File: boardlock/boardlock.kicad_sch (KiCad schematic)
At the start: 0 parts

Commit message: update
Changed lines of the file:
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@@
 (kicad_sch (version 20230121) (generator eeschema)
   (paper "A4")
-  (sheet (at 62.23 140.97) (size 43.18 29.21) (fields_autoplaced)
+  (sheet (at 191.77 77.47) (size 43.18 29.21) (fields_autoplaced)
     (stroke (width 0.1524) (type solid))
     (fill (color 0 0 0 0.0000))
-    (property "Sheetname" "sensors" (at 62.23 140.2584 0)
+    (property "Sheetname" "sensors" (at 191.77 76.7584 0)
       (effects (font (size 1.27 1.27)) (justify left bottom))
     )
-    (property "Sheetfile" "sesnsors.kicad_sch" (at 62.23 170.7646 0)
+    (property "Sheetfile" "sesnsors.kicad_sch" (at 191.77 107.2646 0)
       (effects (font (size 1.27 1.27)) (justify left top))
     )
@@
     )
   )
-  (sheet (at 132.08 93.98) (size 40.64 24.13) (fields_autoplaced)
+  (sheet (at 191.77 128.27) (size 40.64 24.13) (fields_autoplaced)
     (stroke (width 0.1524) (type solid))
     (fill (color 0 0 0 0.0000))
-    (property "Sheetname" "audio" (at 132.08 93.2684 0)
+    (property "Sheetname" "audio" (at 191.77 127.5584 0)
       (effects (font (size 1.27 1.27)) (justify left bottom))
     )
-    (property "Sheetfile" "audio.kicad_sch" (at 132.08 118.6946 0)
+    (property "Sheetfile" "audio.kicad_sch" (at 191.77 152.9846 0)
       (effects (font (size 1.27 1.27)) (justify left top))
     )
@@
     )
   )
-  (sheet (at 60.96 34.29) (size 43.18 30.48) (fields_autoplaced)
+  (sheet (at 187.96 25.4) (size 43.18 30.48) (fields_autoplaced)
     (stroke (width 0.1524) (type solid))
     (fill (color 0 0 0 0.0000))
-    (property "Sheetname" "power" (at 60.96 33.5784 0)
+    (property "Sheetname" "power" (at 187.96 24.6884 0)
       (effects (font (size 1.27 1.27)) (justify left bottom))
     )
-    (property "Sheetfile" "power.kicad_sch" (at 60.96 65.3546 0)
+    (property "Sheetfile" "power.kicad_sch" (at 187.96 56.4646 0)
       (effects (font (size 1.27 1.27)) (justify left top))
     )

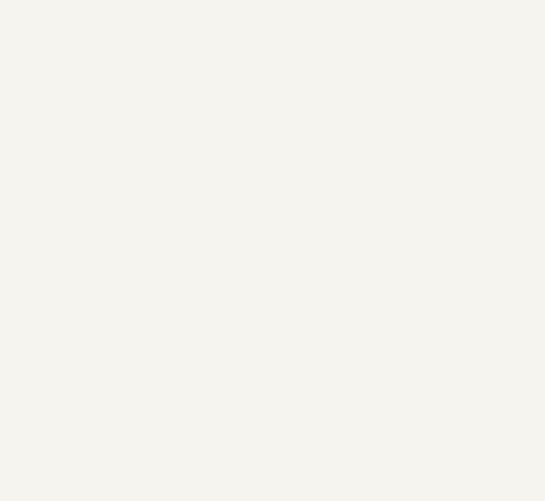
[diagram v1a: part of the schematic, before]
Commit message: Started adding IMU and GPS circuits
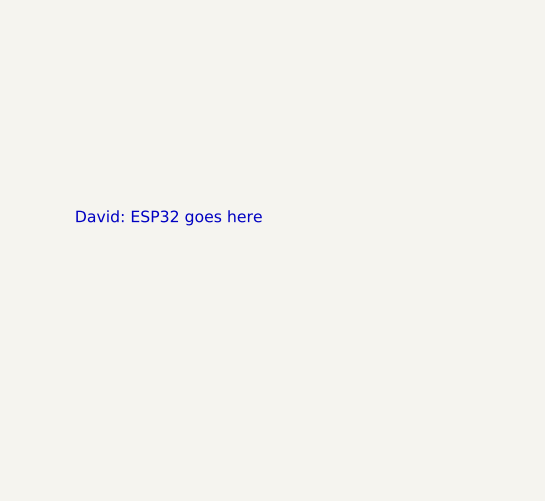
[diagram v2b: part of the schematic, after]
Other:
- note added: "David: ESP32 goes here"
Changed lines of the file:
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@@
 (kicad_sch (version 20230121) (generator eeschema)
   (paper "A4")
+  (text "David: ESP32 goes here" (at 62.23 45.72 0)
+    (effects (font (size 1.27 1.27)) (justify right bottom))
+  )
   (sheet (at 191.77 77.47) (size 43.18 29.21) (fields_autoplaced)
     (stroke (width 0.1524) (type solid))

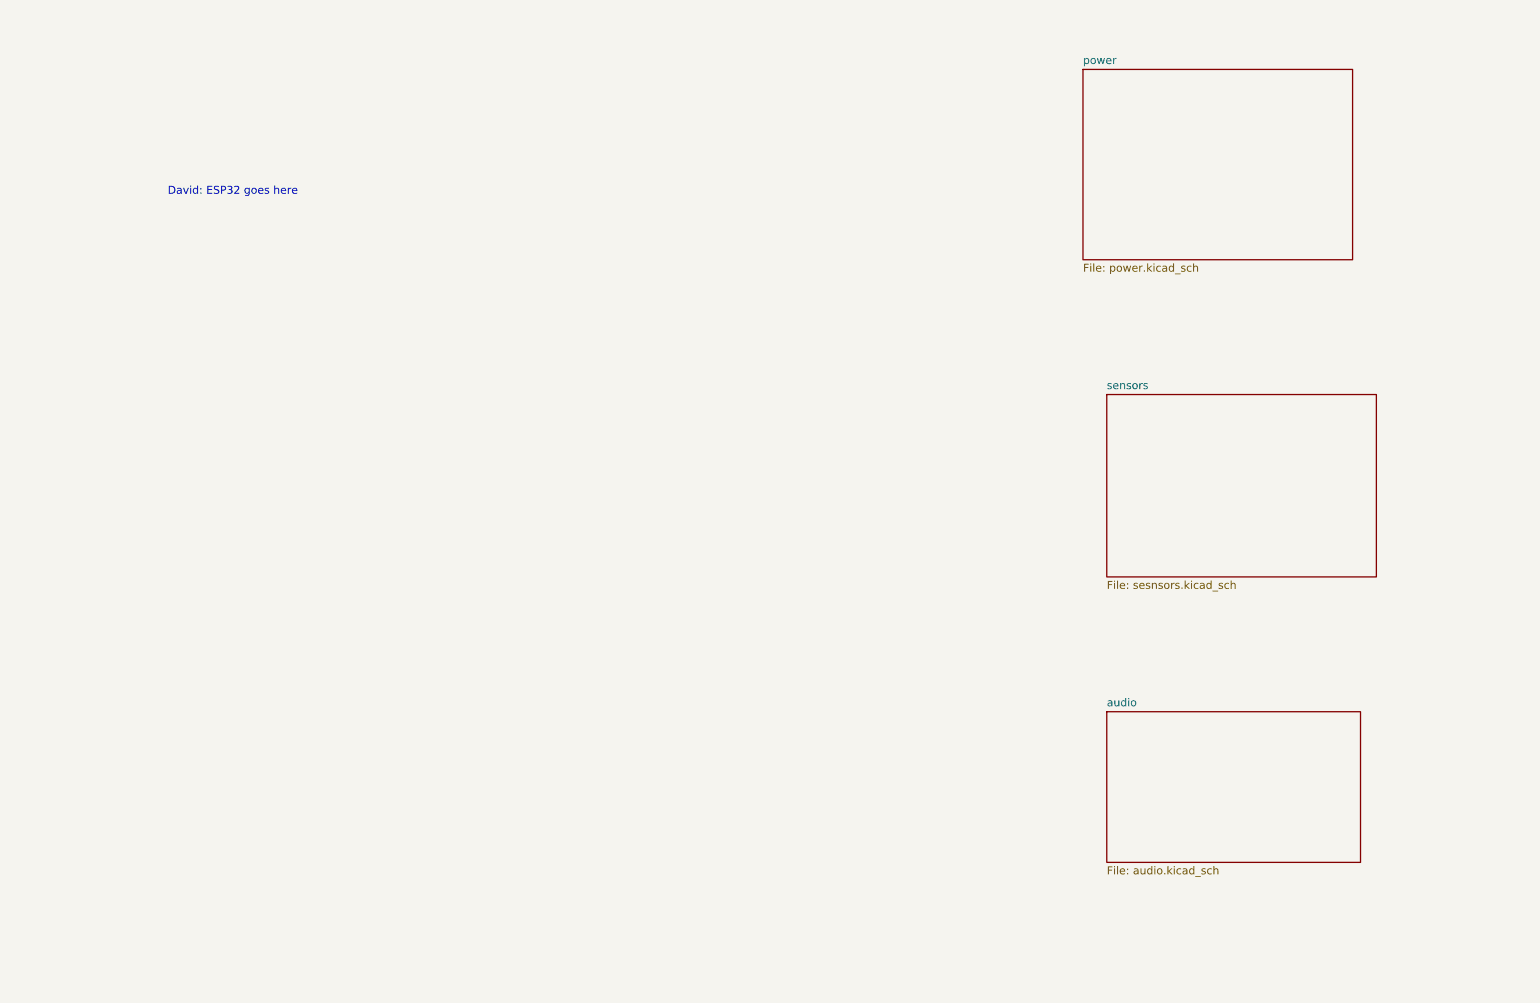
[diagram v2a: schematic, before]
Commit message: fixed some weird file naming issue
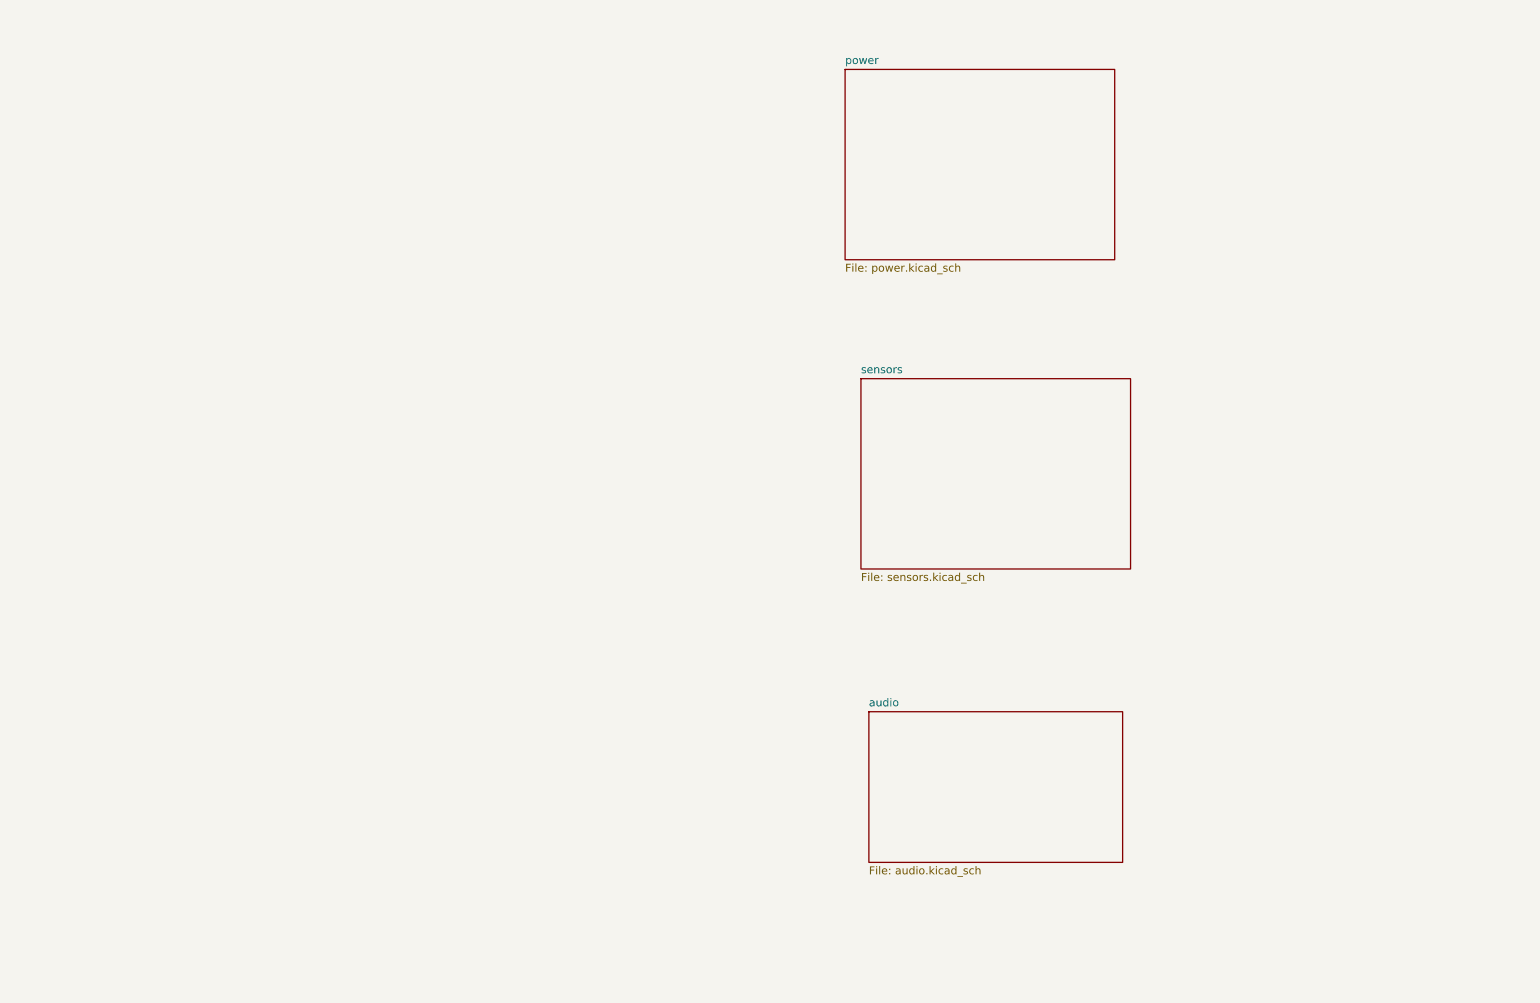
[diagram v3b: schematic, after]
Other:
- sheet sensors: file sesnsors.kicad_sch -> sensors.kicad_sch
- note removed: "David: ESP32 goes here"
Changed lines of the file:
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@@
 (kicad_sch (version 20230121) (generator eeschema)
   (paper "A4")
-  (text "David: ESP32 goes here" (at 62.23 45.72 0)
-    (effects (font (size 1.27 1.27)) (justify right bottom))
-  )
-  (sheet (at 191.77 77.47) (size 43.18 29.21) (fields_autoplaced)
+  (sheet (at 153.67 128.27) (size 40.64 24.13) (fields_autoplaced)
     (stroke (width 0.1524) (type solid))
     (fill (color 0 0 0 0.0000))
-    (property "Sheetname" "sensors" (at 191.77 76.7584 0)
+    (property "Sheetname" "audio" (at 153.67 127.5584 0)
       (effects (font (size 1.27 1.27)) (justify left bottom))
     )
-    (property "Sheetfile" "sesnsors.kicad_sch" (at 191.77 107.2646 0)
-      (effects (font (size 1.27 1.27)) (justify left top))
-    )
-    (instances
-      (project "boardlock"
-        (path "/48f24f42-fd64-4860-9f12-ca34cf195758" (page "2"))
-      )
-    )
-  )
-  (sheet (at 191.77 128.27) (size 40.64 24.13) (fields_autoplaced)
-    (stroke (width 0.1524) (type solid))
-    (fill (color 0 0 0 0.0000))
-    (property "Sheetname" "audio" (at 191.77 127.5584 0)
-      (effects (font (size 1.27 1.27)) (justify left bottom))
-    )
-    (property "Sheetfile" "audio.kicad_sch" (at 191.77 152.9846 0)
+    (property "Sheetfile" "audio.kicad_sch" (at 153.67 152.9846 0)
       (effects (font (size 1.27 1.27)) (justify left top))
     )
@@
         (path "/48f24f42-fd64-4860-9f12-ca34cf195758" (page "4"))
       )
+      (project "boardlock_back"
+        (path "/e1fc29ce-837e-4062-84d8-c7e423f9eab9" (page "4"))
+      )
     )
   )
-  (sheet (at 187.96 25.4) (size 43.18 30.48) (fields_autoplaced)
+  (sheet (at 149.86 25.4) (size 43.18 30.48) (fields_autoplaced)
     (stroke (width 0.1524) (type solid))
     (fill (color 0 0 0 0.0000))
-    (property "Sheetname" "power" (at 187.96 24.6884 0)
+    (property "Sheetname" "power" (at 149.86 24.6884 0)
       (effects (font (size 1.27 1.27)) (justify left bottom))
     )
-    (property "Sheetfile" "power.kicad_sch" (at 187.96 56.4646 0)
+    (property "Sheetfile" "power.kicad_sch" (at 149.86 56.4646 0)
       (effects (font (size 1.27 1.27)) (justify left top))
     )
@@
         (path "/48f24f42-fd64-4860-9f12-ca34cf195758" (page "3"))
       )
+      (project "boardlock_back"
+        (path "/e1fc29ce-837e-4062-84d8-c7e423f9eab9" (page "3"))
+      )
     )
+  )
+  (sheet (at 152.4 74.93) (size 43.18 30.48) (fields_autoplaced)
+    (stroke (width 0.1524) (type solid))
+    (fill (color 0 0 0 0.0000))
+    (property "Sheetname" "sensors" (at 152.4 74.2184 0)
+      (effects (font (size 1.27 1.27)) (justify left bottom))
+    )
+    (property "Sheetfile" "sensors.kicad_sch" (at 152.4 105.9946 0)
+      (effects (font (size 1.27 1.27)) (justify left top))
+    )
+    (instances
+      (project "boardlock"
+        (path "/48f24f42-fd64-4860-9f12-ca34cf195758" (page "3"))
+      )
+      (project "boardlock_back"
+        (path "/e1fc29ce-837e-4062-84d8-c7e423f9eab9" (page "2"))
+      )
+    )
